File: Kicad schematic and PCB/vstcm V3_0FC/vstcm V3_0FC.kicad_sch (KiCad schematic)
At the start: 97 parts, among them IC1 TL3474, IC2 RB-0512D, IC3 MCP4922-E{slash}P, IC4 MCP4922-E{slash}P, IC5 MCP4922-E{slash}P, IC6 TL3474, J1 Conn_01x24_Male, J2 Conn_01x05_Male, J3 Conn_01x25_Male, J6 Conn_01x02_Male, J7 Conn_01x03_Male, J8 Conn_01x01_Male, J9 Conn_01x02_Male, SW1 SW_Push, SW2 SW_Push, SW3 SW_Push, SW4 SW_Push, SW5 SW_Push, U1 Teensy4.1, U3 LP2950-3_3_TO92, U5 LM2940T-5.0

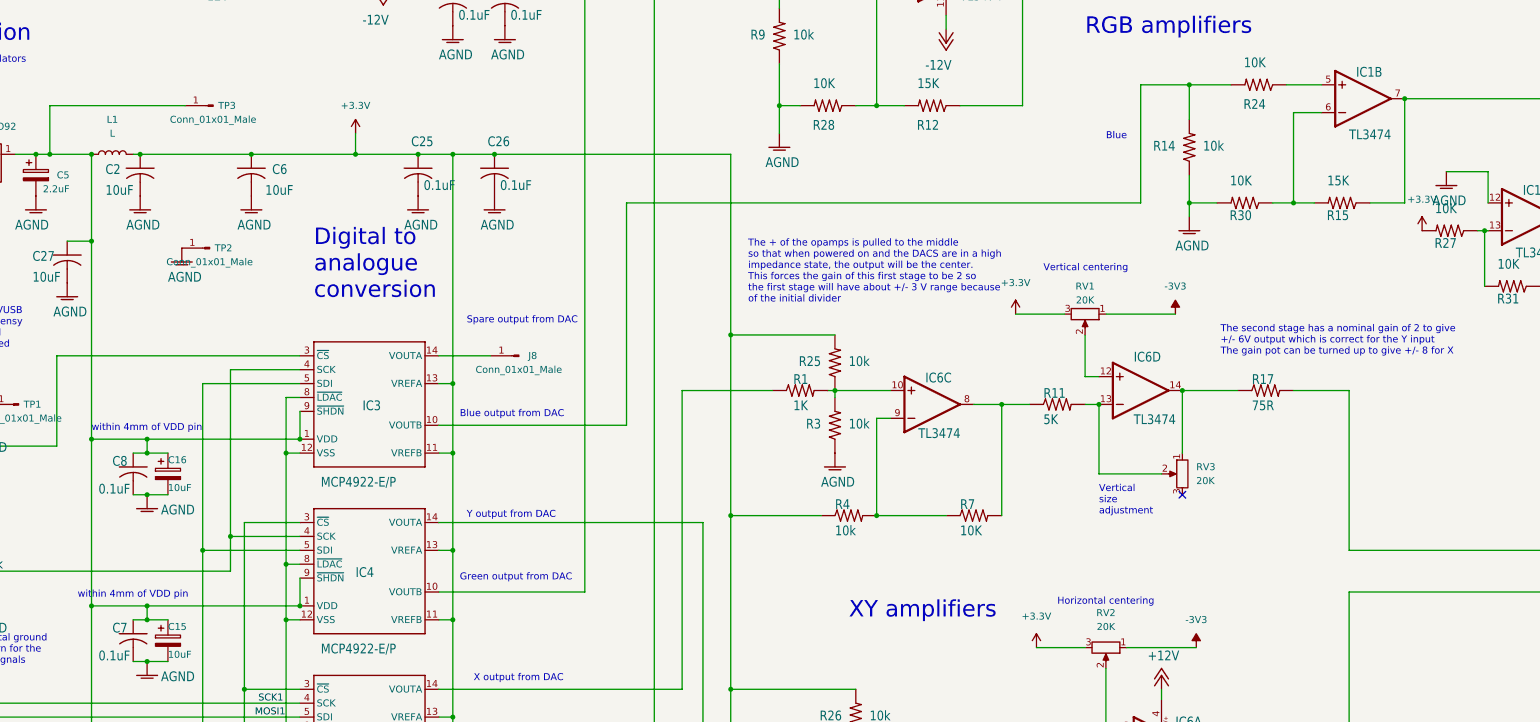
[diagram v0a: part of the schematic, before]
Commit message: More info on type of IC sockets and mounting for Teensy; Kicad files updated to v8.
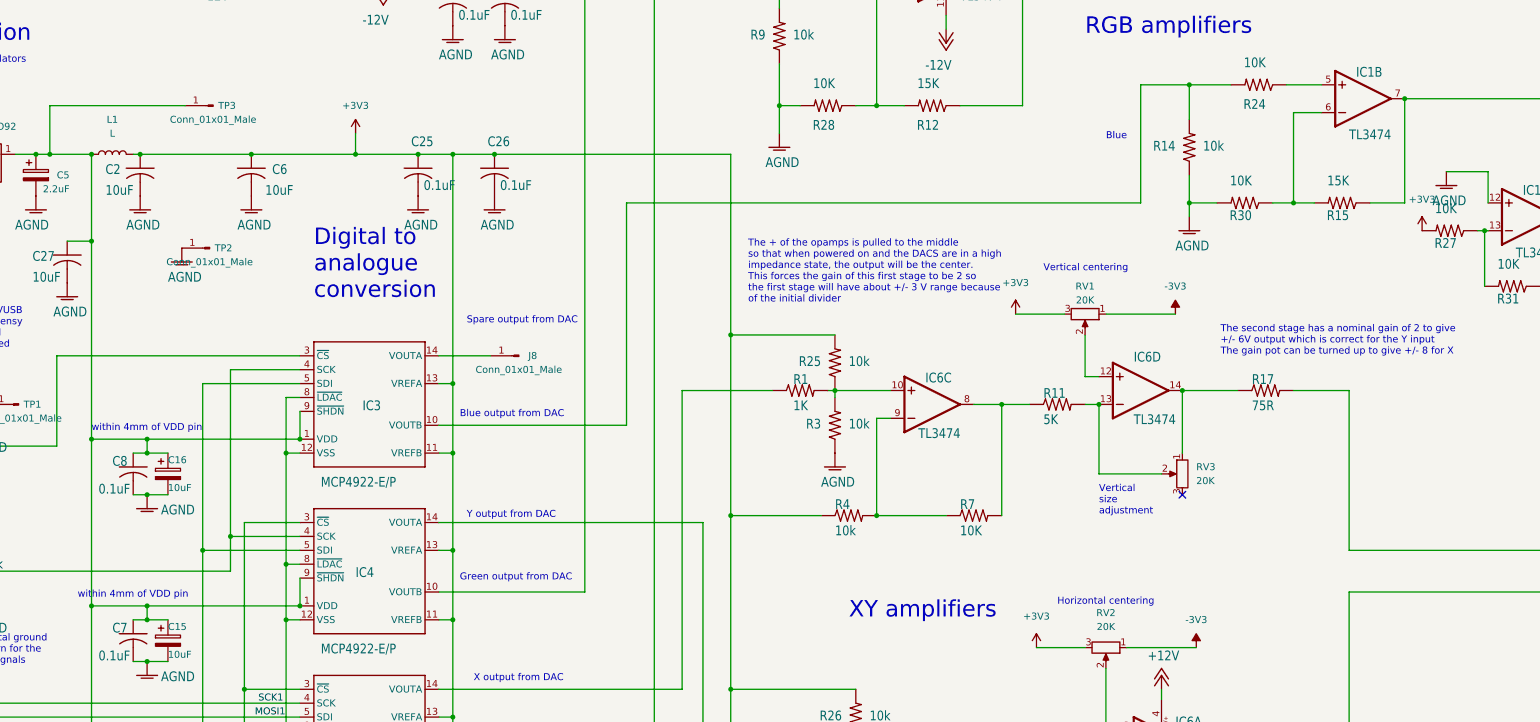
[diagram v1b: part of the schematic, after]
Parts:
- IC3, IC4, IC5: symbol teensyv-eagle-import:MCP4922-E/P -> teensyv-eagle-import:MCP4922-E/P
- R1, R10, R12, R14, R15, R16, R17, R18, R2, R22, R23, R24, R25, R26, R27, R28, R29, R3, R30, R31, R4, R5, R6, R7, R8, R9: symbol teensyv-eagle-import:R-US_0204/2V -> teensyv-eagle-import:R-US_0204/2V
- R11, R13, R19, R20, R21: symbol teensyv-eagle-import:R-US_0204/7 -> teensyv-eagle-import:R-US_0204/7
